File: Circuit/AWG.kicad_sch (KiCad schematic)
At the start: 23 parts, among them J1 Power, J2 Pump 1, J3 Pump 2, J4 Pump 3, J5 WL1, J6 Display, M1 Fan_3pin, M2 Fan_3pin, Q1 RFP30N06LE, Q2 RFP30N06LE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

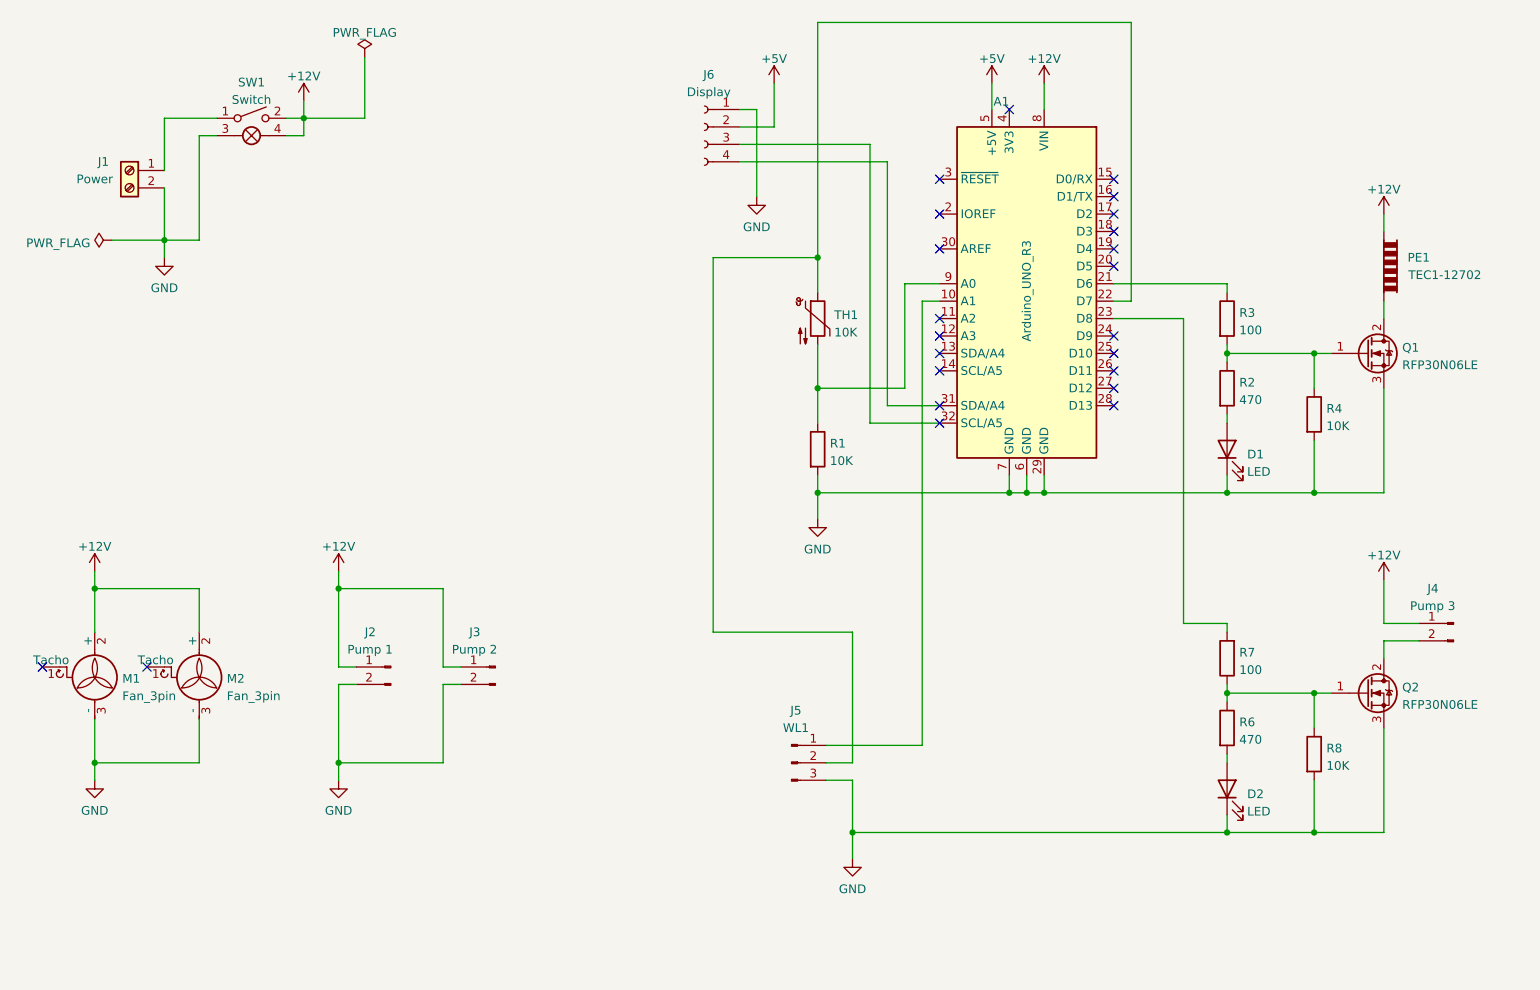
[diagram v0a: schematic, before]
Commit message: [Circuit] Switch to Arduino Nano
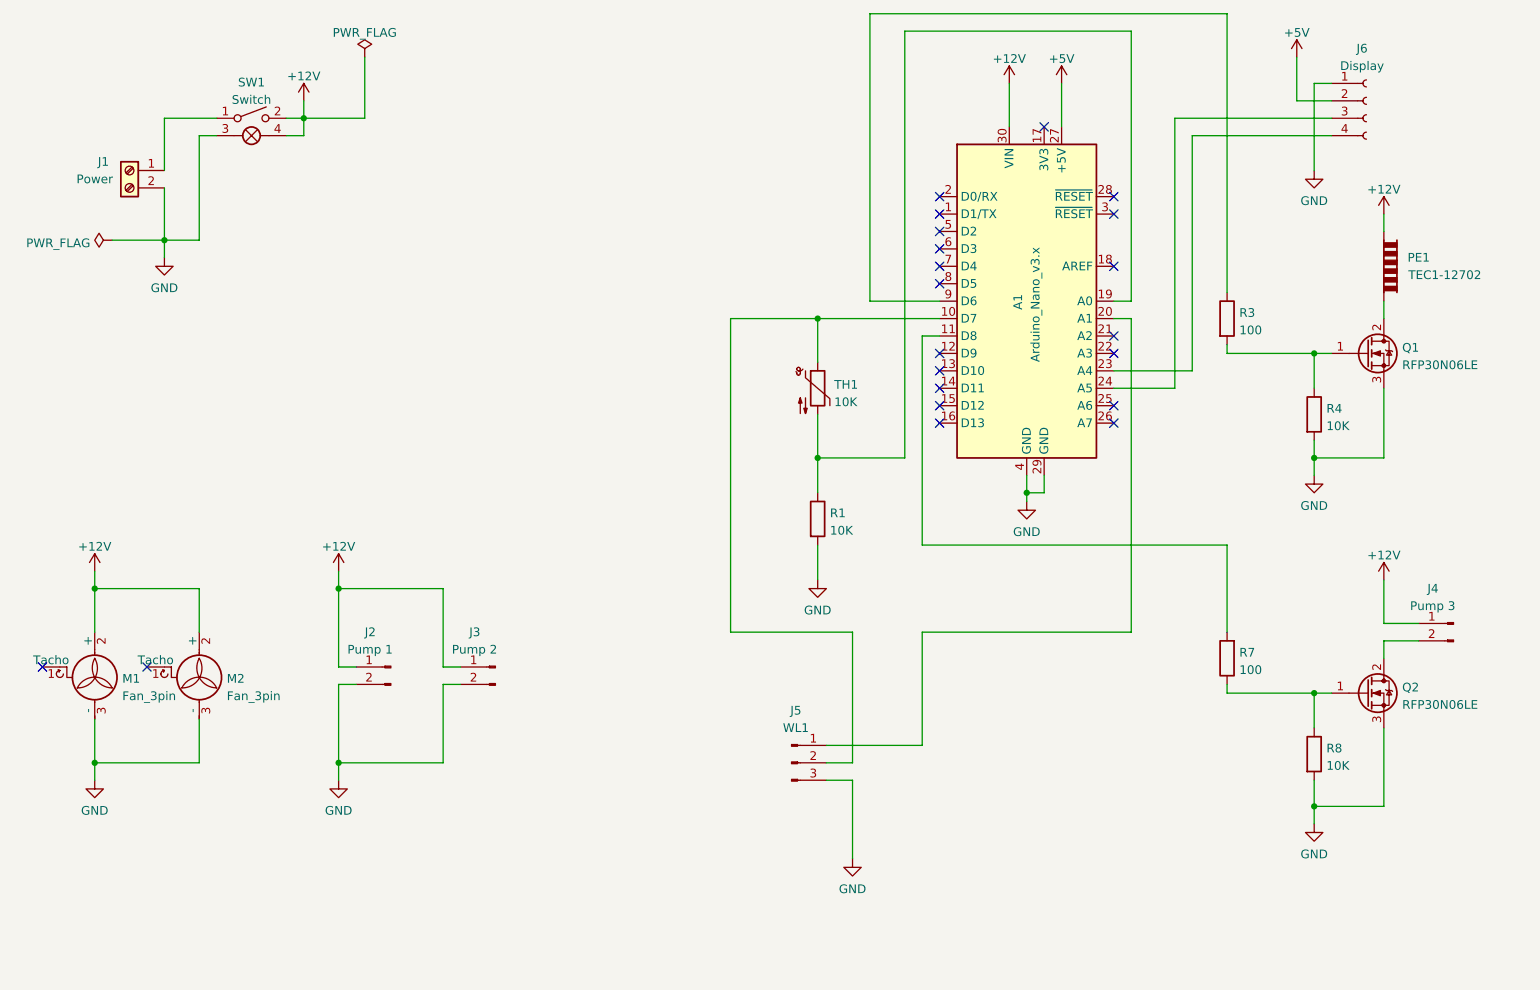
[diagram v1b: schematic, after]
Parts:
- removed A1: Arduino_UNO_R3, Module:Arduino_UNO_R3, symbol MCU_Module:Arduino_UNO_R3
- removed D1, D2: LED, LED_THT:LED_D3.0mm_FlatTop, symbol Device:LED
- removed R2, R6: 470, Resistor_THT:R_Axial_DIN0207_L6.3mm_D2.5mm_P7.62mm_Horizontal, symbol Device:R
- added A1: Arduino_Nano_v3.x, Module:Arduino_Nano, symbol MCU_Module:Arduino_Nano_v3.x
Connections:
- net +12V: now also A1.30 (VIN)
- net +5V: now also A1.27 (+5V)
- net GND: now also A1.29 (GND), A1.4 (GND)
- net at J5.1 (Pin_1): now also A1.20 (A1)
- net at R3.1: now also A1.9 (D6)
- net at J5.2 (Pin_2), TH1.1: now also A1.10 (D7)
- net at R7.2: now also A1.11 (D8)
- net at J6.4 (Pin_4): now also A1.23 (A4)
- net at J6.3 (Pin_3): now also A1.24 (A5)
- net at R1.1, TH1.2: now also A1.19 (A0)
- no-connect marks 23 -> 21
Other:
- moved on the sheet: J6, R1, TH1

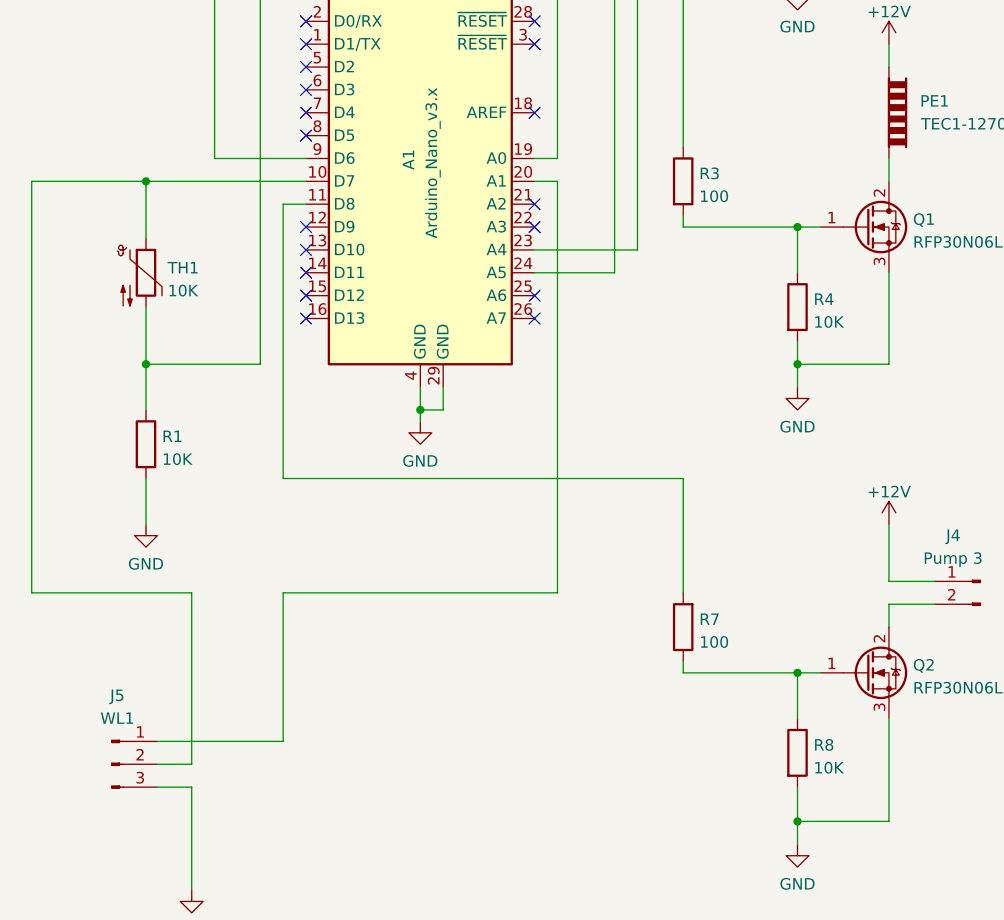
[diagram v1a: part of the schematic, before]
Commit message: [Circuit] Adjust footprints and references
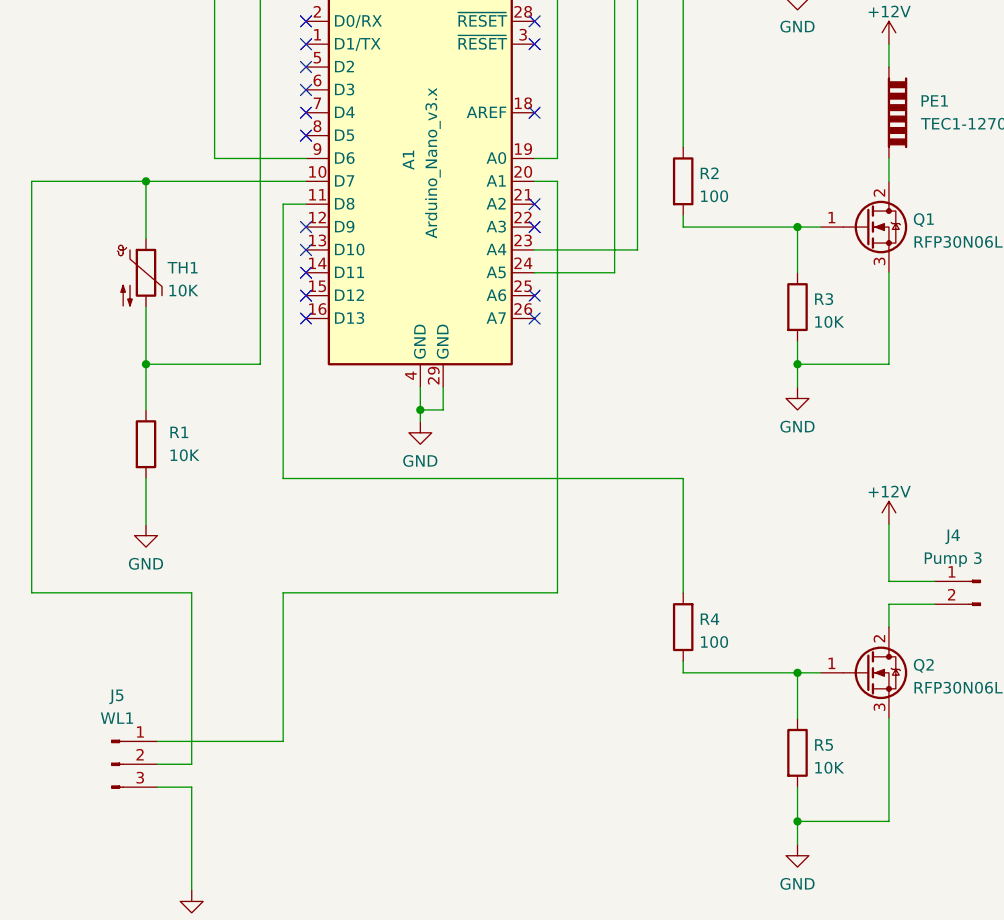
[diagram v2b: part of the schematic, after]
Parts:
- J5: footprint (none) -> Connector_PinHeader_2.54mm:PinHeader_1x03_P2.54mm_Vertical
- M1, M2: footprint Connector_PinHeader_2.54mm:PinHeader_1x03_P2.54mm_Vertical -> Connector_Molex:Molex_KK-254_AE-6410-03A_1x03_P2.54mm_Vertical
- R1: footprint Resistor_THT:R_Axial_DIN0207_L6.3mm_D2.5mm_P7.62mm_Horizontal -> Resistor_THT:R_Axial_DIN0204_L3.6mm_D1.6mm_P7.62mm_Horizontal
- R2: renamed from R3; footprint Resistor_THT:R_Axial_DIN0207_L6.3mm_D2.5mm_P7.62mm_Horizontal -> Resistor_THT:R_Axial_DIN0204_L3.6mm_D1.6mm_P7.62mm_Horizontal
- R3: renamed from R4; footprint Resistor_THT:R_Axial_DIN0207_L6.3mm_D2.5mm_P7.62mm_Horizontal -> Resistor_THT:R_Axial_DIN0204_L3.6mm_D1.6mm_P7.62mm_Horizontal
- R4: renamed from R7; footprint Resistor_THT:R_Axial_DIN0207_L6.3mm_D2.5mm_P7.62mm_Horizontal -> Resistor_THT:R_Axial_DIN0204_L3.6mm_D1.6mm_P7.62mm_Horizontal
- R5: renamed from R8; footprint Resistor_THT:R_Axial_DIN0207_L6.3mm_D2.5mm_P7.62mm_Horizontal -> Resistor_THT:R_Axial_DIN0204_L3.6mm_D1.6mm_P7.62mm_Horizontal
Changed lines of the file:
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@@
   (symbol (lib_id "Device:R") (at 217.17 97.79 0) (unit 1)
     (in_bom yes) (on_board yes) (fields_autoplaced)
-    (property "Reference" "R4" (id 0) (at 218.948 96.9553 0)
+    (property "Reference" "R3" (id 0) (at 218.948 96.9553 0)
       (effects (font (size 1.27 1.27)) (justify left))
     )
@@
       (effects (font (size 1.27 1.27)) (justify left))
     )
-    (property "Footprint" "Resistor_THT:R_Axial_DIN0207_L6.3mm_D2.5mm_P7.62mm_Horizontal" (id 2) (at 215.392 97.79 90)
+    (property "Footprint" "Resistor_THT:R_Axial_DIN0204_L3.6mm_D1.6mm_P7.62mm_Horizontal" (id 2) (at 215.392 97.79 90)
       (effects (font (size 1.27 1.27)) hide)
     )
@@
       (effects (font (size 1.27 1.27)) (justify left))
     )
-    (property "Footprint" "Connector_PinHeader_2.54mm:PinHeader_1x03_P2.54mm_Vertical" (id 2) (at 54.61 136.906 0)
+    (property "Footprint" "Connector_Molex:Molex_KK-254_AE-6410-03A_1x03_P2.54mm_Vertical" (id 2) (at 54.61 136.906 0)
       (effects (font (size 1.27 1.27)) hide)
     )
@@
   (symbol (lib_id "Device:R") (at 204.47 83.82 0) (unit 1)
     (in_bom yes) (on_board yes) (fields_autoplaced)
-    (property "Reference" "R3" (id 0) (at 206.248 82.9853 0)
+    (property "Reference" "R2" (id 0) (at 206.248 82.9853 0)
       (effects (font (size 1.27 1.27)) (justify left))
     )
@@
       (effects (font (size 1.27 1.27)) (justify left))
     )
-    (property "Footprint" "Resistor_THT:R_Axial_DIN0207_L6.3mm_D2.5mm_P7.62mm_Horizontal" (id 2) (at 202.692 83.82 90)
+    (property "Footprint" "Resistor_THT:R_Axial_DIN0204_L3.6mm_D1.6mm_P7.62mm_Horizontal" (id 2) (at 202.692 83.82 90)
       (effects (font (size 1.27 1.27)) hide)
     )
@@
   (symbol (lib_id "Device:R") (at 204.47 133.35 180) (unit 1)
     (in_bom yes) (on_board yes) (fields_autoplaced)
-    (property "Reference" "R7" (id 0) (at 206.248 132.5153 0)
+    (property "Reference" "R4" (id 0) (at 206.248 132.5153 0)
       (effects (font (size 1.27 1.27)) (justify right))
     )
@@
       (effects (font (size 1.27 1.27)) (justify right))
     )
-    (property "Footprint" "Resistor_THT:R_Axial_DIN0207_L6.3mm_D2.5mm_P7.62mm_Horizontal" (id 2) (at 206.248 133.35 90)
+    (property "Footprint" "Resistor_THT:R_Axial_DIN0204_L3.6mm_D1.6mm_P7.62mm_Horizontal" (id 2) (at 206.248 133.35 90)
       (effects (font (size 1.27 1.27)) hide)
     )
@@
   (symbol (lib_id "Device:R") (at 144.78 113.03 0) (unit 1)
     (in_bom yes) (on_board yes) (fields_autoplaced)
-    (property "Reference" "R1" (id 0) (at 146.558 112.1953 0)
-      (effects (font (size 1.27 1.27)) (justify left))
-    )
-    (property "Value" "10K" (id 1) (at 146.558 114.7322 0)
-      (effects (font (size 1.27 1.27)) (justify left))
-    )
-    (property "Footprint" "Resistor_THT:R_Axial_DIN0207_L6.3mm_D2.5mm_P7.62mm_Horizontal" (id 2) (at 143.002 113.03 90)
+    (property "Reference" "R1" (id 0) (at 147.32 111.7599 0)
+      (effects (font (size 1.27 1.27)) (justify left))
+    )
+    (property "Value" "10K" (id 1) (at 147.32 114.2999 0)
+      (effects (font (size 1.27 1.27)) (justify left))
+    )
+    (property "Footprint" "Resistor_THT:R_Axial_DIN0204_L3.6mm_D1.6mm_P7.62mm_Horizontal" (id 2) (at 143.002 113.03 90)
       (effects (font (size 1.27 1.27)) hide)
     )
@@
     (property "Reference" "J5" (id 0) (at 141.605 140.97 0))
     (property "Value" "WL1" (id 1) (at 141.605 143.51 0))
-    (property "Footprint" "" (id 2) (at 140.97 148.59 0)
+    (property "Footprint" "Connector_PinHeader_2.54mm:PinHeader_1x03_P2.54mm_Vertical" (id 2) (at 140.97 148.59 0)
       (effects (font (size 1.27 1.27)) hide)
     )
@@
   (symbol (lib_id "Device:R") (at 217.17 147.32 0) (unit 1)
     (in_bom yes) (on_board yes) (fields_autoplaced)
-    (property "Reference" "R8" (id 0) (at 218.948 146.4853 0)
+    (property "Reference" "R5" (id 0) (at 218.948 146.4853 0)
       (effects (font (size 1.27 1.27)) (justify left))
     )
@@
       (effects (font (size 1.27 1.27)) (justify left))
     )
-    (property "Footprint" "Resistor_THT:R_Axial_DIN0207_L6.3mm_D2.5mm_P7.62mm_Horizontal" (id 2) (at 215.392 147.32 90)
+    (property "Footprint" "Resistor_THT:R_Axial_DIN0204_L3.6mm_D1.6mm_P7.62mm_Horizontal" (id 2) (at 215.392 147.32 90)
       (effects (font (size 1.27 1.27)) hide)
     )
@@
       (effects (font (size 1.27 1.27)) (justify left))
     )
-    (property "Footprint" "Connector_PinHeader_2.54mm:PinHeader_1x03_P2.54mm_Vertical" (id 2) (at 39.37 136.906 0)
+    (property "Footprint" "Connector_Molex:Molex_KK-254_AE-6410-03A_1x03_P2.54mm_Vertical" (id 2) (at 39.37 136.906 0)
       (effects (font (size 1.27 1.27)) hide)
     )
@@
     )
     (path "/ae472c6a-68b0-40da-ad06-e3c270d33133"
-      (reference "J5") (unit 1) (value "WL1") (footprint "")
+      (reference "J5") (unit 1) (value "WL1") (footprint "Connector_PinHeader_2.54mm:PinHeader_1x03_P2.54mm_Vertical")
     )
     (path "/8a69803a-f3bd-4486-ae2e-979612b8450b"
@@
     )
     (path "/c6d538bd-1206-40d1-b447-a7e534cdd7eb"
-      (reference "M1") (unit 1) (value "Fan_3pin") (footprint "Connector_PinHeader_2.54mm:PinHeader_1x03_P2.54mm_Vertical")
+      (reference "M1") (unit 1) (value "Fan_3pin") (footprint "Connector_Molex:Molex_KK-254_AE-6410-03A_1x03_P2.54mm_Vertical")
     )
     (path "/50f3a180-86db-4207-a3a2-1ad7f5209b3e"
-      (reference "M2") (unit 1) (value "Fan_3pin") (footprint "Connector_PinHeader_2.54mm:PinHeader_1x03_P2.54mm_Vertical")
+      (reference "M2") (unit 1) (value "Fan_3pin") (footprint "Connector_Molex:Molex_KK-254_AE-6410-03A_1x03_P2.54mm_Vertical")
     )
     (path "/857c0455-6977-4d97-842a-605dd29ce838"
@@
     )
     (path "/aa2d7a59-1b2b-46e4-b2bf-3ebd4f565706"
-      (reference "R1") (unit 1) (value "10K") (footprint "Resistor_THT:R_Axial_DIN0207_L6.3mm_D2.5mm_P7.62mm_Horizontal")
+      (reference "R1") (unit 1) (value "10K") (footprint "Resistor_THT:R_Axial_DIN0204_L3.6mm_D1.6mm_P7.62mm_Horizontal")
     )
     (path "/56df4a7b-0b9e-4aed-b778-cb4f42e33e3d"
-      (reference "R3") (unit 1) (value "100") (footprint "Resistor_THT:R_Axial_DIN0207_L6.3mm_D2.5mm_P7.62mm_Horizontal")
+      (reference "R2") (unit 1) (value "100") (footprint "Resistor_THT:R_Axial_DIN0204_L3.6mm_D1.6mm_P7.62mm_Horizontal")
     )
     (path "/4f910016-3781-48c0-b0a9-219f2333b055"
-      (reference "R4") (unit 1) (value "10K") (footprint "Resistor_THT:R_Axial_DIN0207_L6.3mm_D2.5mm_P7.62mm_Horizontal")
+      (reference "R3") (unit 1) (value "10K") (footprint "Resistor_THT:R_Axial_DIN0204_L3.6mm_D1.6mm_P7.62mm_Horizontal")
     )
     (path "/5d21e03a-1e09-400f-9153-9e2f23755df2"
-      (reference "R7") (unit 1) (value "100") (footprint "Resistor_THT:R_Axial_DIN0207_L6.3mm_D2.5mm_P7.62mm_Horizontal")
+      (reference "R4") (unit 1) (value "100") (footprint "Resistor_THT:R_Axial_DIN0204_L3.6mm_D1.6mm_P7.62mm_Horizontal")
     )
     (path "/bacbda9f-6673-4183-8b09-c84715486139"
-      (reference "R8") (unit 1) (value "10K") (footprint "Resistor_THT:R_Axial_DIN0207_L6.3mm_D2.5mm_P7.62mm_Horizontal")
+      (reference "R5") (unit 1) (value "10K") (footprint "Resistor_THT:R_Axial_DIN0204_L3.6mm_D1.6mm_P7.62mm_Horizontal")
     )
     (path "/90dc3aaf-96f4-4132-b4e7-9d4e94cb6ca5"
